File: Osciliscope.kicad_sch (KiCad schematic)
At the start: 25 parts, among them J1 U.FL, J2 Conn_01x04_Socket, J3 U.FL, J4 Conn_01x04_Socket, SW1 SW_Rotary_1x8_MP, SW2 SW_Rotary_1x8_MP, U1 MCP1700x-330xxMB, U2 ADC082S101, U5 TLV9061xDBV, U7 TLV9061xDBV, U8 MCP4251-104E/ML-ND

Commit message: PCB design
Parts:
- added C10, C9: 1u, Capacitor_SMD:C_1206_3216Metric, symbol Device:C
- added D1, D2, D3, D4: D, Diode_SMD:D_0201_0603Metric, symbol Device:D
- added SW3, SW4: SW_Nidec_CAS-120A1, Button_Switch_SMD:Nidec_Copal_CAS-120A, symbol Switch:SW_Nidec_CAS-120A1
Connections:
- net 3.3Vo is gone; now on net V3.3: C3.1, U2.2 (V_{A})
- net GND: now also D2.2 (A), D4.2 (A)
- net V3.3: now also D1.1 (K), D3.1 (K)
- net at J1.1 (In), R10.1: now also C9.1, SW3.3 (A); no longer R3.2
- net at J3.1 (In), R14.1: now also C10.1, SW4.3 (A); no longer R4.2
- new net: D3.2 (A), D4.1 (K), R4.2, SW4.2 (B)
- new net: C10.2, SW4.1 (C)
- new net: D1.2 (A), D2.1 (K), R3.2, SW3.2 (B)
- new net: C9.2, SW3.1 (C)
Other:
- moved on the sheet: J1, J3, R10, R14, R3, R4, U5, U7

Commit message: USBC PD
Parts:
- added C11: 1uF, Capacitor_SMD:C_1206_3216Metric, symbol Device:C
- added C12, C13: 10u, Capacitor_SMD:C_1206_3216Metric, symbol Device:C
- added D5: Red, PCM_JLCPCB:D_0805, symbol PCM_JLCPCB-Diodes:LED,0805,Red
- added J5: USB_C_Receptacle_USB2.0_14P, Connector_USB:USB_C_Receptacle_Amphenol_124019772112A, symbol Connector:USB_C_Receptacle_USB2.0_14P
- added J6: Conn_01x02_MountingPin, symbol Connector_Generic_MountingPin:Conn_01x02_MountingPin
- added R13: 10k, Capacitor_SMD:C_0603_1608Metric, symbol Device:R
- added U3: IP2721, Package_SO:TSSOP-16_4.4x5mm_P0.65mm, symbol Interface_USB:IP2721
- added U4: AZ1084-5.0, Package_TO_SOT_SMD:TO-252-2, symbol Regulator_Linear:AZ1084-5.0
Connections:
- net 5Vin: now also C13.1, D5.2, J6.1 (Pin_1), U4.2 (VO)
- net GND: now also C11.2, C12.2, C13.2, J5.A1 (GND), J5.A12 (GND), J5.B1 (GND), J5.B12 (GND), J5.S1 (SHIELD), J6.2 (Pin_2), R13.1, U3.5 (GND), U4.1 (GND)
- new net: J5.A5 (CC1), U3.13 (CC1)
- new net: J5.B5 (CC2), U3.12 (CC2)
- new net: D5.1, R13.2
- new net USBCRAW: C11.1, C12.1, J5.A4 (VBUS), J5.A9 (VBUS), J5.B4 (VBUS), J5.B9 (VBUS), U3.11 (SEL), U3.16 (VBUS), U3.2 (VIN), U4.3 (VI)

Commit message: forgot to save the schematic lol
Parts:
- removed C11, C2: 1uF, Capacitor_SMD:C_1206_3216Metric, symbol Device:C
- removed C12, C13: 10u, Capacitor_SMD:C_1206_3216Metric, symbol Device:C
- removed D5: Red, PCM_JLCPCB:D_0805, symbol PCM_JLCPCB-Diodes:LED,0805,Red
- removed J5: USB_C_Receptacle_USB2.0_14P, Connector_USB:USB_C_Receptacle_Amphenol_124019772112A, symbol Connector:USB_C_Receptacle_USB2.0_14P
- removed J6: Conn_01x02_MountingPin, symbol Connector_Generic_MountingPin:Conn_01x02_MountingPin
- removed R13: 10k, Capacitor_SMD:C_0603_1608Metric, symbol Device:R
- removed U3: IP2721, Package_SO:TSSOP-16_4.4x5mm_P0.65mm, symbol Interface_USB:IP2721
- removed U4: AZ1084-5.0, Package_TO_SOT_SMD:TO-252-2, symbol Regulator_Linear:AZ1084-5.0

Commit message: more small changes
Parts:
- C10, C9: value 1u -> 1uF
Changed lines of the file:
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@@
 			)
 		)
-		(property "Datasheet" "https://eecs.engineering.oregonstate.edu/education/inventory_datasheets/P1502744917.pdf"
+		(property "Datasheet" "https://mm.digikey.com/Volume0/opasdata/d220001/medias/docus/609/CL05A105KO5NNNC_Spec_5-2-19.pdf"
 			(at 143.51 92.71 0)
 			(effects
@@
 			)
 		)
-		(property "Datasheet" "https://eecs.engineering.oregonstate.edu/education/inventory_datasheets/P1502744917.pdf"
+		(property "Datasheet" "https://mm.digikey.com/Volume0/opasdata/d220001/medias/docus/609/CL05A105KO5NNNC_Spec_5-2-19.pdf"
 			(at 149.86 48.26 0)
 			(effects
@@
 			)
 		)
-		(property "Datasheet" "https://eecs.engineering.oregonstate.edu/education/inventory_datasheets/P1502744917.pdf"
+		(property "Datasheet" "https://mm.digikey.com/Volume0/opasdata/d220001/medias/docus/609/CL05A105KO5NNNC_Spec_5-2-19.pdf"
 			(at 129.54 54.61 0)
 			(effects
@@
 			)
 		)
-		(property "Datasheet" "https://eecs.engineering.oregonstate.edu/education/inventory_datasheets/P1502744917.pdf"
+		(property "Datasheet" "https://mm.digikey.com/Volume0/opasdata/d220001/medias/docus/609/CL05A105KO5NNNC_Spec_5-2-19.pdf"
 			(at 129.54 62.23 0)
 			(effects
@@
 			)
 		)
-		(property "Datasheet" "https://eecs.engineering.oregonstate.edu/education/inventory_datasheets/P1502744917.pdf"
+		(property "Datasheet" "https://mm.digikey.com/Volume0/opasdata/d220001/medias/docus/609/CL05A105KO5NNNC_Spec_5-2-19.pdf"
 			(at 212.09 48.26 0)
 			(effects
@@
 			)
 		)
-		(property "Value" "1u"
+		(property "Value" "1uF"
 			(at 38.1 53.34 90)
 			(effects
@@
 			)
 		)
-		(property "Datasheet" "~"
+		(property "Datasheet" "https://mm.digikey.com/Volume0/opasdata/d220001/medias/docus/609/CL05A105KO5NNNC_Spec_5-2-19.pdf"
 			(at 38.1 58.42 0)
 			(effects
@@
 			)
 		)
-		(property "Datasheet" "~"
+		(property "Datasheet" "https://yageogroup.com/content/datasheet/asset/file/PYU-RT_1-TO-0-01_ROHS_L"
 			(at 68.58 60.96 0)
 			(effects
@@
 			)
 		)
-		(property "Datasheet" "~"
+		(property "Datasheet" "https://industrial.panasonic.com/cdbs/www-data/pdf/RDM0000/AOA0000C307.pdf"
 			(at 27.94 54.61 0)
 			(effects
@@
 			)
 		)
-		(property "Datasheet" "~"
+		(property "Datasheet" "https://www.vishay.com/docs/20035/dcrcwe3.pdf"
 			(at 119.38 54.61 0)
 			(effects
@@
 			)
 		)
-		(property "Datasheet" "~"
+		(property "Datasheet" "https://yageogroup.com/content/datasheet/asset/file/PYU-RT_1-TO-0-01_ROHS_L"
 			(at 69.85 91.44 0)
 			(effects
@@
 			)
 		)
-		(property "Datasheet" "~"
+		(property "Datasheet" "https://industrial.panasonic.com/cdbs/www-data/pdf/RDM0000/AOA0000C307.pdf"
 			(at 29.21 85.09 0)
 			(effects
@@
 			)
 		)
-		(property "Datasheet" "https://eecs.engineering.oregonstate.edu/education/inventory_datasheets/P1502744917.pdf"
+		(property "Datasheet" "https://mm.digikey.com/Volume0/opasdata/d220001/medias/docus/609/CL05A105KO5NNNC_Spec_5-2-19.pdf"
 			(at 201.93 48.26 0)
 			(effects
@@
 			)
 		)
-		(property "Datasheet" "https://eecs.engineering.oregonstate.edu/education/inventory_datasheets/P1502744917.pdf"
+		(property "Datasheet" "https://mm.digikey.com/Volume0/opasdata/d220001/medias/docus/609/CL05A105KO5NNNC_Spec_5-2-19.pdf"
 			(at 190.5 48.26 0)
 			(effects
@@
 			)
 		)
-		(property "Datasheet" "~"
+		(property "Datasheet" "https://www.vishay.com/docs/20035/dcrcwe3.pdf"
 			(at 119.38 62.23 0)
 			(effects
@@
 			)
 		)
-		(property "Value" "1u"
+		(property "Value" "1uF"
 			(at 35.56 83.82 90)
 			(effects
@@
 			)
 		)
-		(property "Datasheet" "~"
+		(property "Datasheet" "https://mm.digikey.com/Volume0/opasdata/d220001/medias/docus/609/CL05A105KO5NNNC_Spec_5-2-19.pdf"
 			(at 35.56 88.9 0)
 			(effects

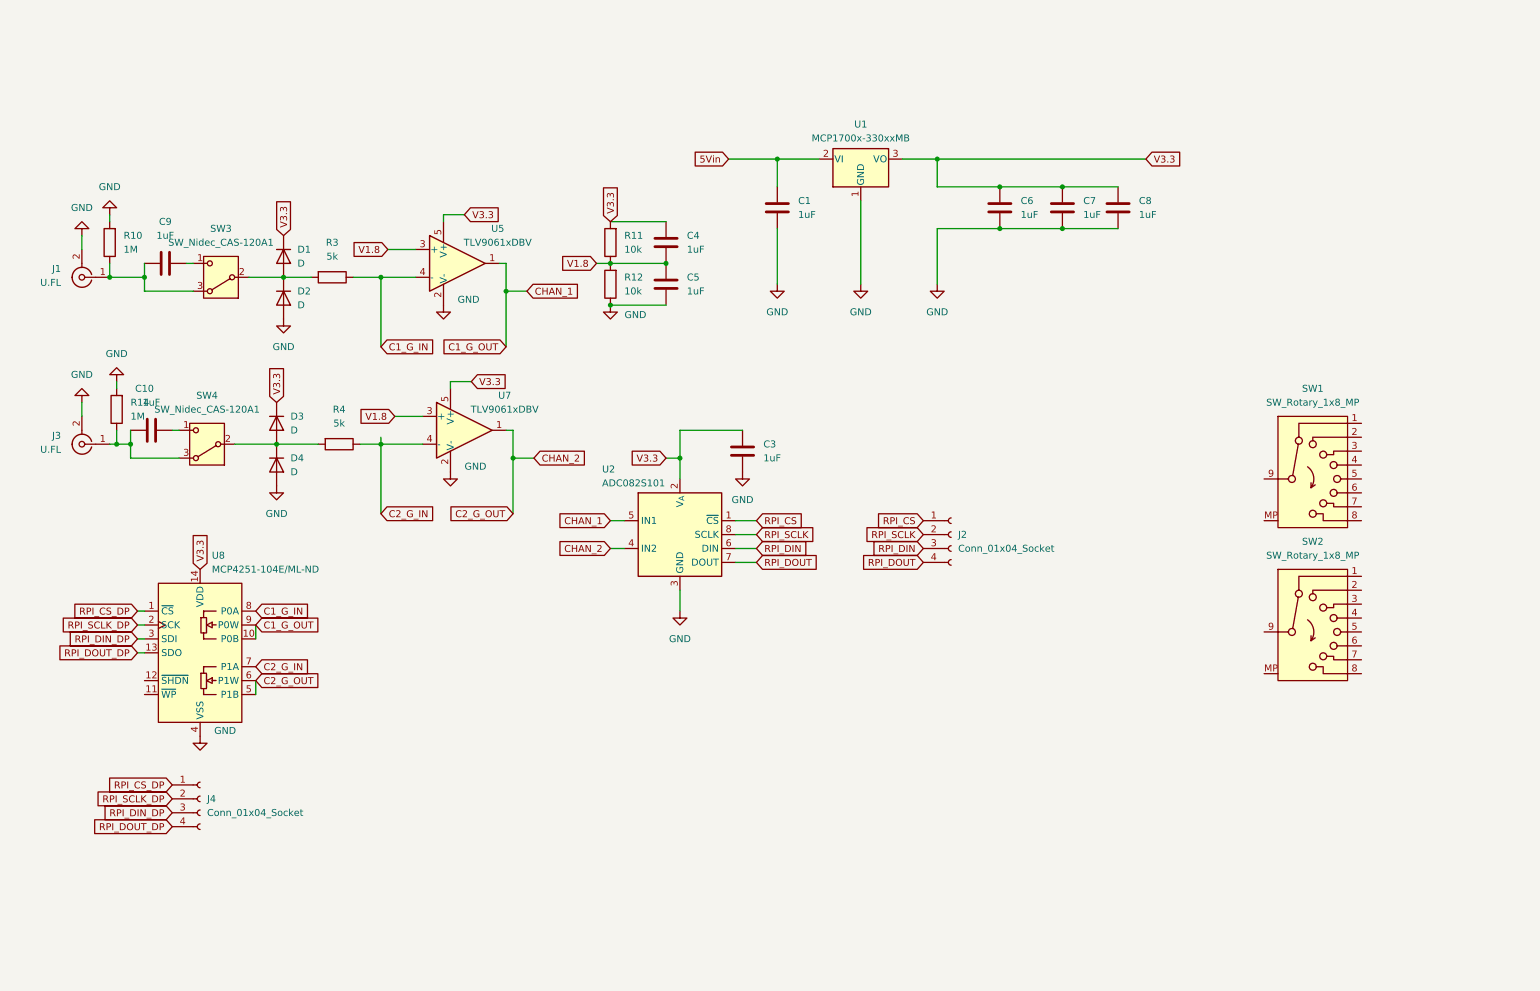
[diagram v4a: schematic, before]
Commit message: Revert "forgot to save the schematic lol"
This reverts commit 07f5faf1676d518d9647f621f39270092870860e.
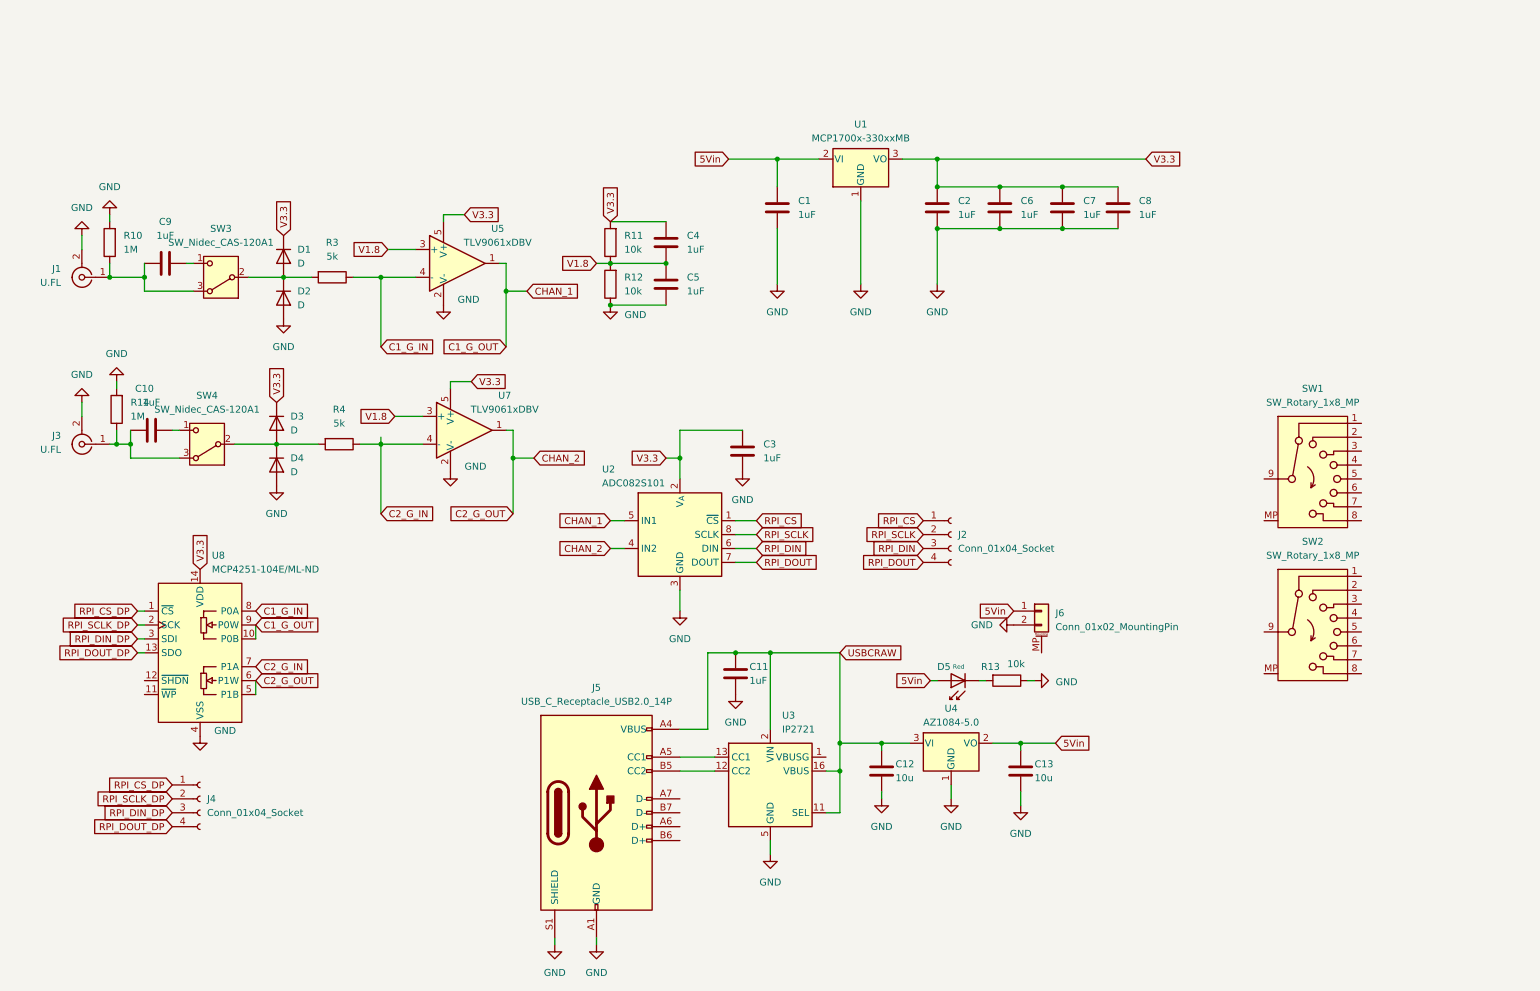
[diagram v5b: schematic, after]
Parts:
- added C11, C2: 1uF, Capacitor_SMD:C_1206_3216Metric, symbol Device:C
- added C12, C13: 10u, Capacitor_SMD:C_1206_3216Metric, symbol Device:C
- added D5: Red, PCM_JLCPCB:D_0805, symbol PCM_JLCPCB-Diodes:LED,0805,Red
- added J5: USB_C_Receptacle_USB2.0_14P, Connector_USB:USB_C_Receptacle_Amphenol_124019772112A, symbol Connector:USB_C_Receptacle_USB2.0_14P
- added J6: Conn_01x02_MountingPin, symbol Connector_Generic_MountingPin:Conn_01x02_MountingPin
- added R13: 10k, Capacitor_SMD:C_0603_1608Metric, symbol Device:R
- added U3: IP2721, Package_SO:TSSOP-16_4.4x5mm_P0.65mm, symbol Interface_USB:IP2721
- added U4: AZ1084-5.0, Package_TO_SOT_SMD:TO-252-2, symbol Regulator_Linear:AZ1084-5.0
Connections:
- net 5Vin: now also C13.1, D5.2, J6.1 (Pin_1), U4.2 (VO)
- net GND: now also C11.2, C12.2, C13.2, C2.2, J5.A1 (GND), J5.A12 (GND), J5.B1 (GND), J5.B12 (GND), J5.S1 (SHIELD), J6.2 (Pin_2), R13.1, U3.5 (GND), U4.1 (GND)
- net V3.3: now also C2.1
- new net: J5.A5 (CC1), U3.13 (CC1)
- new net: J5.B5 (CC2), U3.12 (CC2)
- new net: D5.1, R13.2
- new net USBCRAW: C11.1, C12.1, J5.A4 (VBUS), J5.A9 (VBUS), J5.B4 (VBUS), J5.B9 (VBUS), U3.11 (SEL), U3.16 (VBUS), U3.2 (VIN), U4.3 (VI)

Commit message: encoder circuit added to main
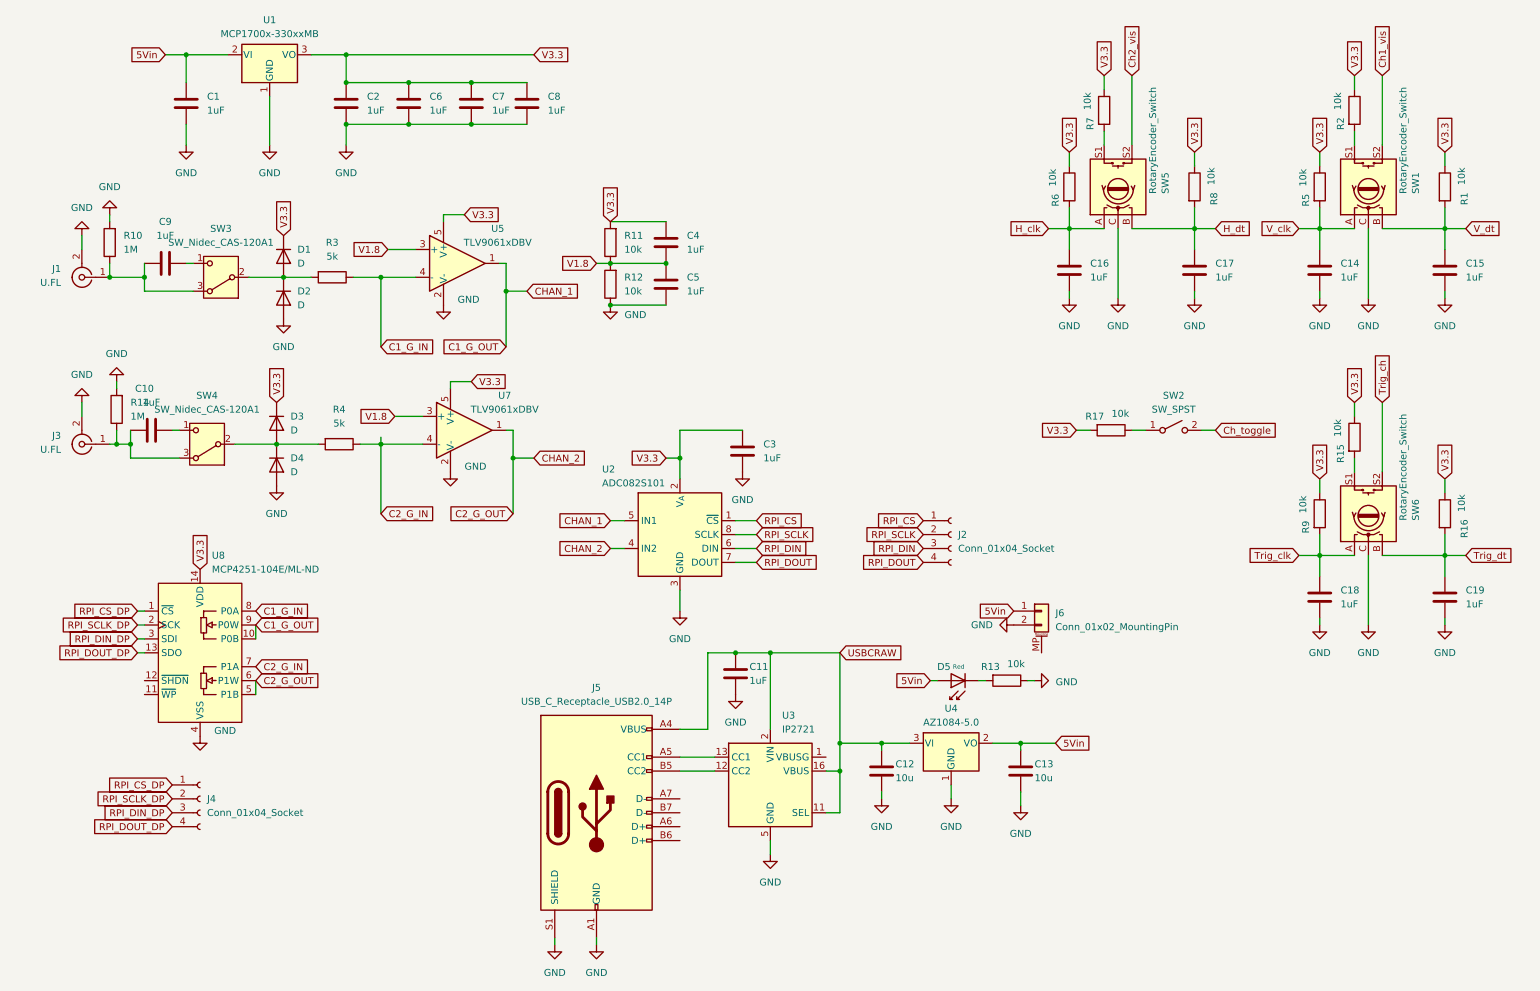
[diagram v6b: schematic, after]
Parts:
- removed SW1, SW2: SW_Rotary_1x8_MP, Rotary_Encoder:RotaryEncoder_Alps_EC11E-Switch_Vertical_H20mm_CircularMountingHoles, symbol Switch:SW_Rotary_1x8_MP
- added C14, C15, C16, C17, C18, C19: 1uF, Capacitor_SMD:C_1206_3216Metric, symbol Device:C
- added R1, R15, R16, R17, R2, R5, R6, R7, R8, R9: 10k, Capacitor_SMD:C_0603_1608Metric, symbol Device:R
- added SW1, SW5, SW6: RotaryEncoder_Switch, Rotary_Encoder:RotaryEncoder_Alps_EC11E-Switch_Vertical_H20mm, symbol Device:RotaryEncoder_Switch
- added SW2: SW_SPST, symbol Switch:SW_SPST
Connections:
- net GND: now also C14.2, C15.2, C16.2, C17.2, C18.2, C19.2, SW1.C, SW5.C, SW6.C
- net V3.3: now also R1.1, R15.1, R16.1, R17.2, R2.1, R5.1, R6.1, R7.1, R8.1, R9.1
- new net: R17.1, SW2.1 (A)
- new net: R15.2, SW6.S1
- new net: R2.2, SW1.S1
- new net: R7.2, SW5.S1
- new net Ch1_vis: SW1.S2
- new net Ch2_vis: SW5.S2
- new net Ch_toggle: SW2.2 (B)
- new net H_clk: C16.1, R6.2, SW5.A
- new net H_dt: C17.1, R8.2, SW5.B
- new net Trig_ch: SW6.S2
- new net Trig_clk: C18.1, R9.2, SW6.A
- new net Trig_dt: C19.1, R16.2, SW6.B
- new net V_clk: C14.1, R5.2, SW1.A
- new net V_dt: C15.1, R1.2, SW1.B
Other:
- moved on the sheet: C1, C2, C6, C7, C8, U1

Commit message: Balls
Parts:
- removed D1, D2, D3, D4: D, Diode_SMD:D_0201_0603Metric, symbol Device:D
- removed J1: U.FL, Connector_Coaxial:BNC_Amphenol_031-5539_Vertical, symbol PCM_JLCPCB-Extended:RF, Connector, U.FL
- removed R10: 1M, Capacitor_SMD:C_0603_1608Metric, symbol Device:R
- added J7: U.FL, Connector_Coaxial:BNC_Amphenol_031-5539_Vertical, symbol PCM_JLCPCB-Extended:RF, Connector, U.FL
- added R18, R19: 1M, Capacitor_SMD:C_0603_1608Metric, symbol Device:R
- added R20: 100k, Capacitor_SMD:C_0603_1608Metric, symbol Device:R
- R14: value 1M -> 100k
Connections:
- net GND: now also J7.2 (Ext), R20.2
- net at C10.1, R14.1, SW4.3 (A): now also R18.1; no longer J3.1 (In)
- net at C9.1, SW3.3 (A): now also R19.1, R20.1
- net at R3.2: no longer SW3.2 (B)
- new net: J7.1 (In), R19.2
- new net: J3.1 (In), R18.2
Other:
- moved on the sheet: C10, R14, SW4
